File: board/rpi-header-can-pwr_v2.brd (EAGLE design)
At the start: 87 x 56.5 mm, 43 parts, among them U1 MCP2515, X1 RJ45-8L21-S, X2 RASPI_BOARD_B+#_E3

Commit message: add board temp sensor add battery voltage sensor
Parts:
- added C13, C15: 100n, rcl:C0603
- added C14: 1u, rcl:C0603
- added R7: 0, resistor:R0603
- added R8, R9: 4.7K, resistor:R0603
- added U2: ADS1015, SparkFun-IC-Conversion:MSOP10
- added U3: BME280, SparkFun-Sensors:LGA-8-2.5X2.5
- moved R4 25.5 mm to (24.5, 52.5), turned to 90 degrees
- moved D2 21.6 mm to (21.0, 49.0), turned to 90 degrees
- moved D3 15.8 mm to (24.5, 47.5), turned to 180 degrees
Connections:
- new net ADC_ALERT: R7.1, X2.40
- new net ADC_INPUT_1: U2.4
- new net I2C_SCL: R9.2, U2.10, U3.4, X2.5
- new net I2C_SDA: R8.2, U2.9, U3.3, X2.3
- new net N$9: R7.2, U2.2
- net +3V3: now also C13.1, C14.1, C15.1, R8.1, R9.1, U2.8, U3.2, U3.6, U3.8
- net GND: now also C13.2, C14.2, C15.2, U2.1, U2.3, U3.1, U3.5, U3.7
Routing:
- net I2C_SCL: track 0.00 -> 71.5 mm, vias 0 -> 2
- net I2C_SDA: track 0.00 -> 62.5 mm
- net +3V3: track 178.3 -> 227.6 mm, vias 2 -> 3
- net N$9: track 0.00 -> 24.1 mm
- net ADC_ALERT: track 0.00 -> 11.6 mm
- net 5V: track 33.3 -> 22.7 mm
- net GND: track 13.7 -> 21.1 mm, vias 203 -> 211
- net TAMPER: track 34.2 -> 39.6 mm
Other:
- board text added: "ADC ALERT"
- board text added: "ADS1x15"
- board text added: "BME280"
- board text added: "T2"
- board text added: "i2c pullups"

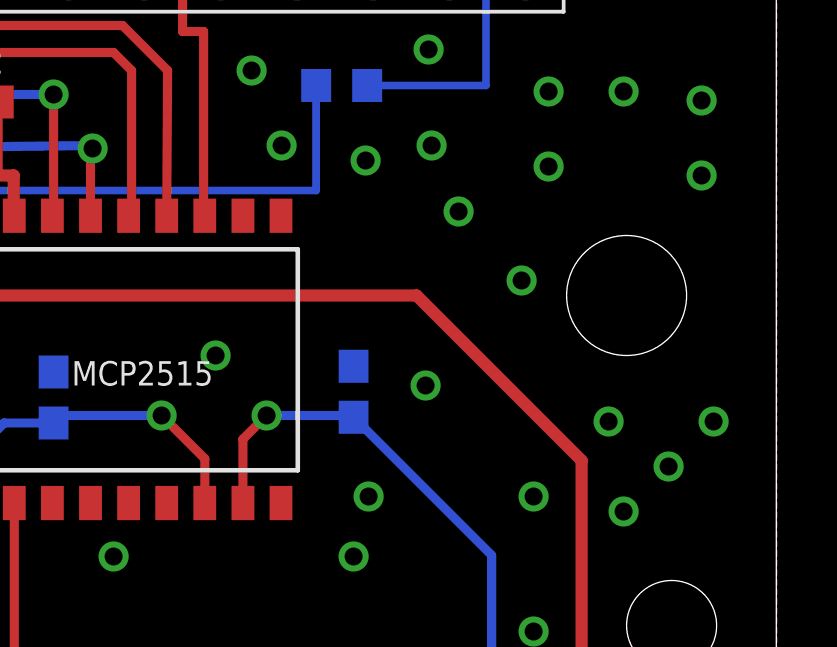
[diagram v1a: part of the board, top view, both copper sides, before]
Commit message: ADC ALERT requires pull up
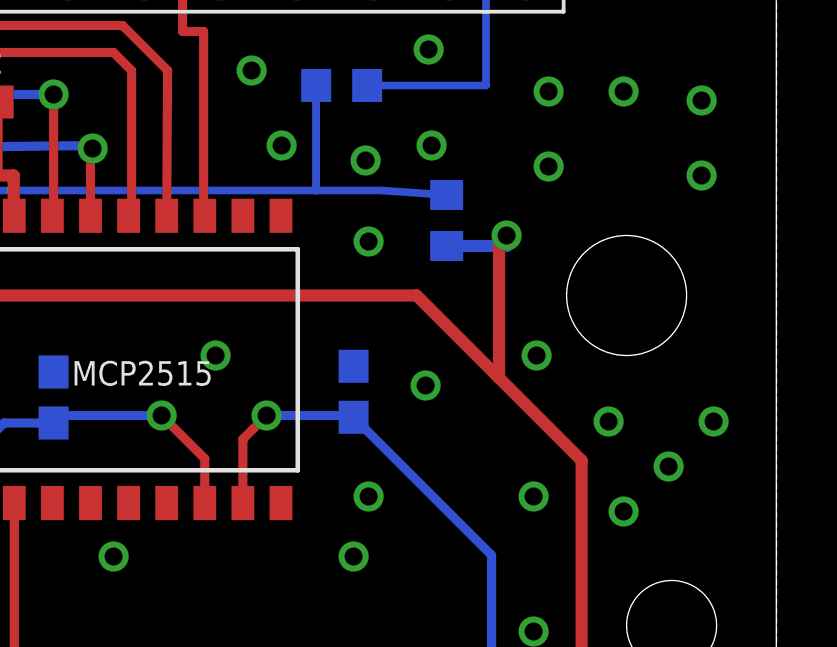
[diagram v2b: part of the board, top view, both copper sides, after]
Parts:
- added R10: 4.7K, resistor:R0603
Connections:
- net +3V3: now also R10.2
- net N$9: now also R10.1
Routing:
- net +3V3: track 227.6 -> 234.9 mm, vias 3 -> 4
- net N$9: track 24.1 -> 28.5 mm
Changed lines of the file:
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@@
 <text x="5.3" y="52.7" size="1.4224" layer="122" rot="MR270">12V</text>
 <text x="18.5" y="48.8" size="1.4224" layer="122" rot="MR90">GND</text>
+<text x="76.4" y="40.3" size="0.8128" layer="122" rot="MR0">R1</text>
 </plain>
 <attributes>
@@
 <element name="C14" library="rcl" package="C0603" value="1u" x="31.5" y="21" rot="MR0"/>
 <element name="C15" library="rcl" package="C0603" value="100n" x="31.54" y="18.82" rot="MR0"/>
+<element name="R10" library="resistor" package="R0603" value="4.7K" x="76" y="43" rot="MR270"/>
 </elements>
 <signals>
@@
 <wire x1="77.5" y1="24.5" x2="80.5" y2="24.5" width="0.4064" layer="1"/>
 <wire x1="80.5" y1="24.5" x2="80.5" y2="35" width="0.4064" layer="1"/>
-<wire x1="80.5" y1="35" x2="75" y2="40.5" width="0.4064" layer="1"/>
+<wire x1="80.5" y1="35" x2="77.75" y2="37.75" width="0.4064" layer="1"/>
+<wire x1="77.75" y1="37.75" x2="75" y2="40.5" width="0.4064" layer="1"/>
 <wire x1="75" y1="40.5" x2="60.32" y2="40.5" width="0.4064" layer="1"/>
 <wire x1="60.32" y1="40.5" x2="60.32" y2="43.1579" width="0.4064" layer="1"/>
@@
 <via x="26" y="25" extent="1-16" drill="0.6"/>
 <wire x1="26" y1="25" x2="26" y2="26.5" width="0.254" layer="1"/>
+<contactref element="R10" pad="2"/>
+<wire x1="76" y1="42.15" x2="78" y2="42.15" width="0.4064" layer="16"/>
+<wire x1="78" y1="42.15" x2="78" y2="42.5" width="0.4064" layer="16"/>
+<via x="78" y="42.5" extent="1-16" drill="0.6"/>
+<wire x1="78" y1="42.5" x2="77.75" y2="42.5" width="0.4064" layer="1"/>
+<wire x1="77.75" y1="42.5" x2="77.75" y2="37.75" width="0.4064" layer="1"/>
 </signal>
 <signal name="GND">
@@
 <via x="81.9" y="47.3" extent="1-16" drill="0.6"/>
 <via x="79.4" y="44.8" extent="1-16" drill="0.6"/>
-<via x="76.4" y="43.3" extent="1-16" drill="0.6"/>
+<via x="73.4" y="42.3" extent="1-16" drill="0.6"/>
 <via x="83.4" y="34.8" extent="1-16" drill="0.6"/>
 <via x="84.9" y="36.3" extent="1-16" drill="0.6"/>
@@
 <via x="85" y="18.6" extent="1-16" drill="0.6"/>
 <via x="84.5" y="44.5" extent="1-16" drill="0.6"/>
-<via x="78.5" y="41" extent="1-16" drill="0.6"/>
+<via x="79" y="38.5" extent="1-16" drill="0.6"/>
 <via x="47.9" y="48.9" extent="1-16" drill="0.6"/>
 <via x="35.9" y="38.4" extent="1-16" drill="0.6"/>
@@
 <wire x1="54.5" y1="44" x2="71.65" y2="44" width="0.254" layer="16"/>
 <wire x1="71.65" y1="44" x2="71.65" y2="47.5" width="0.254" layer="16"/>
+<contactref element="R10" pad="1"/>
+<wire x1="76" y1="43.85" x2="73.85" y2="44" width="0.254" layer="16"/>
+<wire x1="73.85" y1="44" x2="71.65" y2="44" width="0.254" layer="16"/>
 </signal>
 </signals>

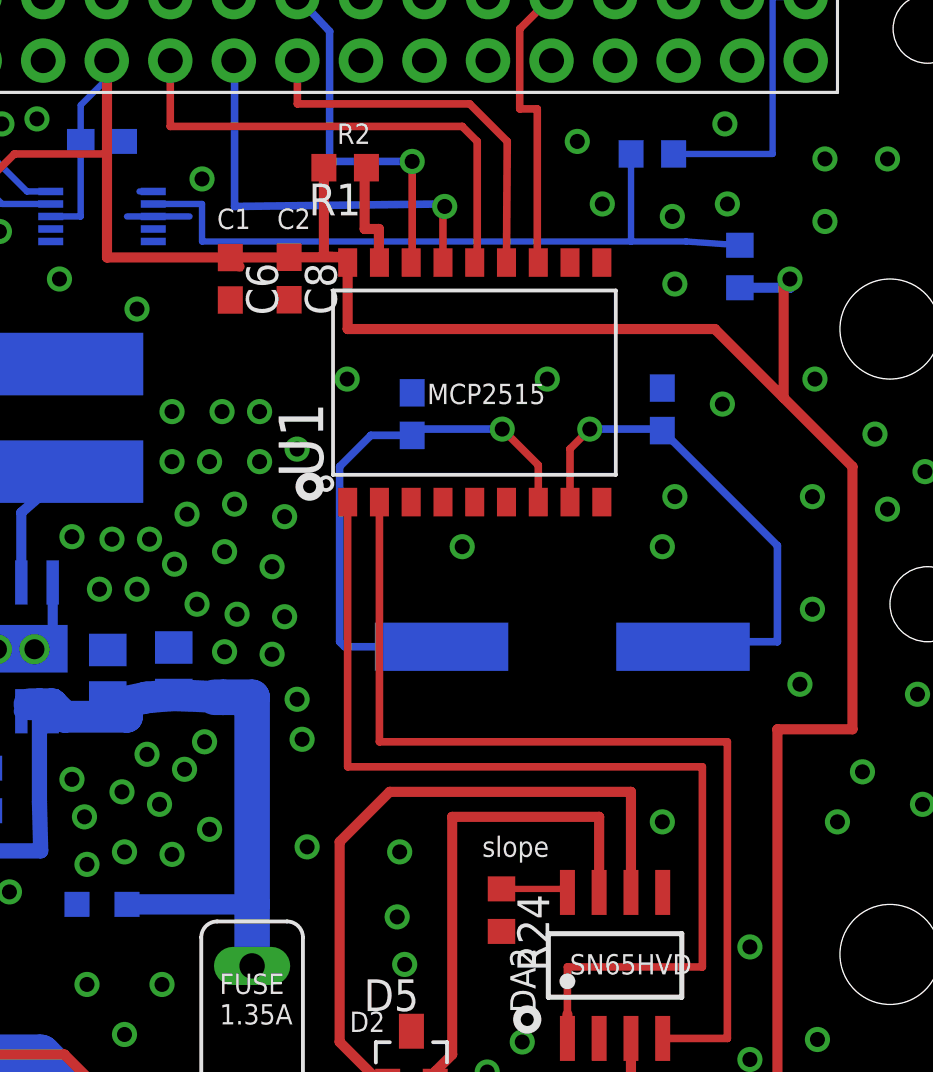
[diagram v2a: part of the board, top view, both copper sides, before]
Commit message: add voltage divider and gpio protection to battery voltage sensor
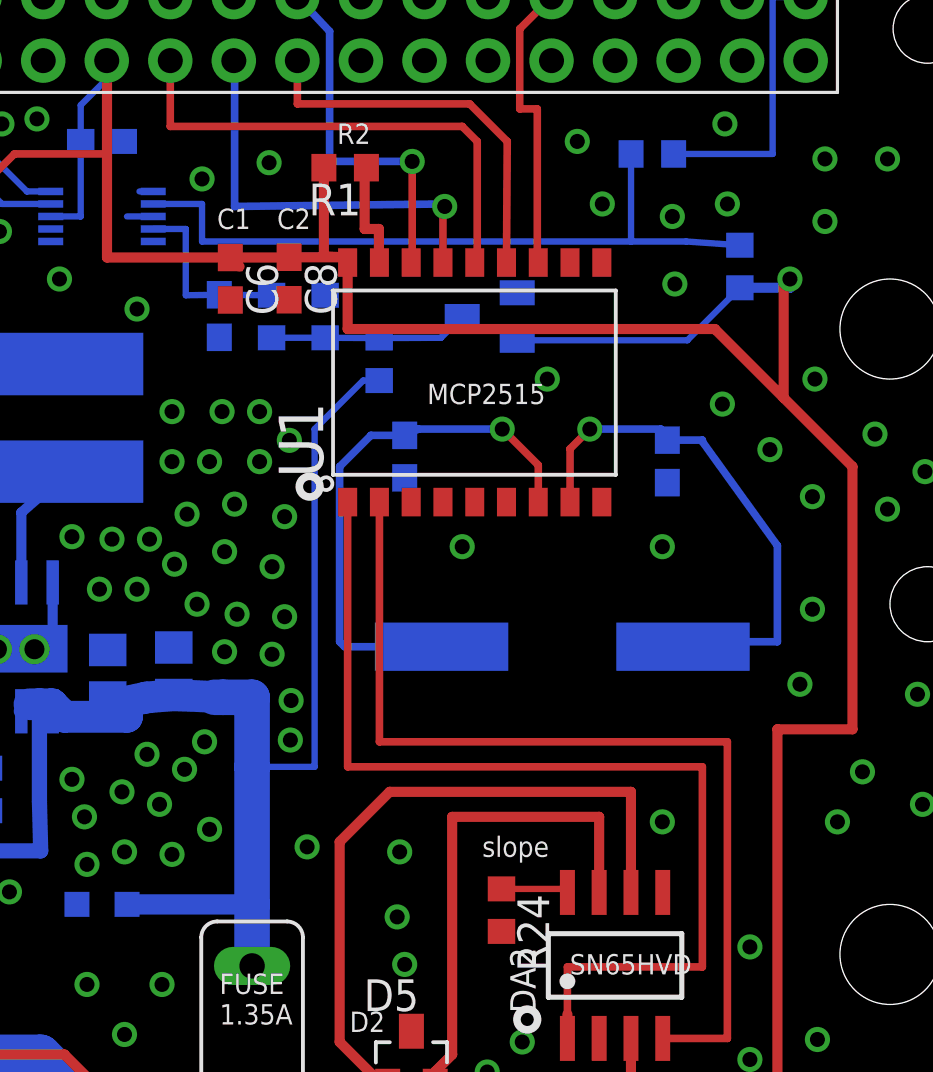
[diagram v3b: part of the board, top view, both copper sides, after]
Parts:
- added C29: 10nF, eagle-ltspice:C0603
- added D7: BAS70-04, diode:SOT23
- added R20: 68k, rcl:R0603
- added R21: 20k, rcl:R0603
- added R22: 1k, rcl:R0603
- moved C2 2.09 mm to (73.1, 35.2), turned to 90 degrees
- moved C1 1.73 mm to (62.6, 35.4), turned to 90 degrees
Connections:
- new net 12V_REFERENCE4: D7.3, R20.2, R21.2, R22.1
- net +12V: now also R20.1
- net +3V3: now also D7.2
- net ADC_INPUT_1: now also C29.2, R22.2
- net GND: now also C29.1, D7.1, R21.1
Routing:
- net +12V: track 75.9 -> 95.3 mm
- net +3V3: track 234.9 -> 244.7 mm
- net 12V_REFERENCE4: track 0.00 -> 7.97 mm
- net ADC_INPUT_1: track 0.00 -> 7.38 mm
- net GND: track 21.1 -> 19.6 mm
- net N$2: track 20.4 -> 20.9 mm
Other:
- board text added: "R13"
- board text added: "R14"
- board text added: "crystal cap"
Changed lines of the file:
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@@
 <text x="18.5" y="48.8" size="1.4224" layer="122" rot="MR90">GND</text>
 <text x="76.4" y="40.3" size="0.8128" layer="122" rot="MR0">R1</text>
+<text x="55.97" y="38.36" size="0.8128" layer="122" rot="MR0">C9</text>
+<text x="58.14" y="38.3" size="0.8128" layer="122" rot="MR0">R5</text>
+<text x="67.25" y="38.21" size="0.8128" layer="122" rot="MR0">D4</text>
+<text x="62.52" y="41.29" size="0.8128" layer="122" rot="MR0">R13</text>
+<text x="60.46" y="42.73" size="0.8128" layer="122" rot="MR0">R14</text>
+<text x="70.75" y="34.21" size="0.8128" layer="122" rot="MR0">crystal cap</text>
 </plain>
 <attributes>
@@
 <attribute name="PROD_ID" value="IC-09906" x="65.4" y="39.64" size="1.778" layer="27" display="off"/>
 </element>
-<element name="C1" library="SparkFun-Capacitors" package="0603-CAP" value="22pF" x="62.9" y="37.1" rot="MR270">
-<attribute name="PROD_ID" value="CAP-07876" x="61.63" y="44.72" size="1.778" layer="28" rot="MR270" display="off"/>
-</element>
-<element name="C2" library="SparkFun-Capacitors" package="0603-CAP" value="22pF" x="72.9" y="37.29" rot="MR270">
-<attribute name="PROD_ID" value="CAP-07876" x="75.44" y="48.72" size="1.778" layer="28" rot="MR270" display="off"/>
+<element name="C1" library="SparkFun-Capacitors" package="0603-CAP" value="22pF" x="62.6" y="35.4" rot="MR90">
+<attribute name="PROD_ID" value="CAP-07876" x="63.87" y="27.78" size="1.778" layer="28" rot="MR90" display="off"/>
+</element>
+<element name="C2" library="SparkFun-Capacitors" package="0603-CAP" value="22pF" x="73.1" y="35.21" rot="MR90">
+<attribute name="PROD_ID" value="CAP-07876" x="70.56" y="23.78" size="1.778" layer="28" rot="MR90" display="off"/>
 </element>
 <element name="C3" library="rcl" package="C0603" value="100n" x="72.48" y="8.87" rot="R270"/>
@@
 <element name="C15" library="rcl" package="C0603" value="100n" x="31.54" y="18.82" rot="MR0"/>
 <element name="R10" library="resistor" package="R0603" value="4.7K" x="76" y="43" rot="MR270"/>
+<element name="R20" library="rcl" package="R0603" value="68k" x="61.58" y="39.29" rot="MR90"/>
+<element name="R21" library="rcl" package="R0603" value="20k" x="59.42" y="41" rot="MR270"/>
+<element name="D7" library="diode" package="SOT23" value="BAS70-04" x="66" y="41" rot="MR270"/>
+<element name="C29" library="eagle-ltspice" package="C0603" value="10nF" x="55.19" y="41.02" rot="MR90">
+<attribute name="SPICEPREFIX" value="C" x="45.19" y="41.02" size="1.778" layer="28" rot="MR90" display="off"/>
+<attribute name="SPICEMODEL" value="NONE" x="45.19" y="41.02" size="1.778" layer="28" rot="MR90" display="off"/>
+</element>
+<element name="R22" library="rcl" package="R0603" value="1k" x="57.28" y="41" rot="MR90"/>
 </elements>
 <signals>
@@
 <wire x1="78" y1="42.5" x2="77.75" y2="42.5" width="0.4064" layer="1"/>
 <wire x1="77.75" y1="42.5" x2="77.75" y2="37.75" width="0.4064" layer="1"/>
+<contactref element="D7" pad="2"/>
+<wire x1="67.1" y1="40.05" x2="73.9" y2="40.05" width="0.254" layer="16"/>
+<wire x1="73.9" y1="40.05" x2="76" y2="42.15" width="0.254" layer="16"/>
 </signal>
 <signal name="GND">
@@
 <contactref element="D3" pad="2"/>
 <via x="62.4" y="19.6" extent="1-16" drill="0.6"/>
-<via x="58.3" y="35.7" extent="1-16" drill="0.6"/>
+<via x="57.99" y="36.05" extent="1-16" drill="0.6"/>
 <via x="41.8" y="26" extent="1-16" drill="0.6"/>
 <via x="42.8" y="27.5" extent="1-16" drill="0.6"/>
@@
 <via x="53.3" y="19.5" extent="1-16" drill="0.6"/>
 <via x="44.3" y="18" extent="1-16" drill="0.6"/>
-<via x="58.5" y="24.1" extent="1-16" drill="0.6"/>
+<via x="58.03" y="24.07" extent="1-16" drill="0.6"/>
 <via x="57.8" y="29" extent="1-16" drill="0.6"/>
 <via x="79.1" y="12.1" extent="1-16" drill="0.6"/>
@@
 <via x="72.3" y="2" extent="1-16" drill="0.6"/>
 <via x="62.3" y="3" extent="1-16" drill="0.6"/>
-<via x="60.3" y="38.5" extent="1-16" drill="0.6"/>
+<via x="77.2" y="35.68" extent="1-16" drill="0.6"/>
 <via x="68.3" y="38.5" extent="1-16" drill="0.6"/>
 <via x="75.3" y="37.5" extent="1-16" drill="0.6"/>
@@
 <contactref element="D18" pad="1"/>
 <contactref element="X1" pad="8"/>
-<via x="58.3" y="25.7" extent="1-16" drill="0.6"/>
+<via x="58.06" y="25.65" extent="1-16" drill="0.6"/>
 <via x="54.6" y="24" extent="1-16" drill="0.6"/>
 <via x="62.6" y="15.1" extent="1-16" drill="0.6"/>
@@
 <via x="81.9" y="33.3" extent="1-16" drill="0.6"/>
 <via x="72.9" y="31.8" extent="1-16" drill="0.6"/>
-<via x="73.4" y="33.8" extent="1-16" drill="0.6"/>
+<via x="57.18" y="47.15" extent="1-16" drill="0.6"/>
 <via x="64.9" y="31.8" extent="1-16" drill="0.6"/>
 <via x="78.9" y="33.8" extent="1-16" drill="0.6"/>
@@
 <contactref element="U2" pad="3"/>
 <contactref element="U2" pad="1"/>
-<wire x1="52.55" y1="45" x2="54" y2="45" width="0.254" layer="16"/>
 <wire x1="52.55" y1="45" x2="51.5" y2="45" width="0.254" layer="16"/>
 <wire x1="52.55" y1="46" x2="52" y2="46" width="0.254" layer="16"/>
@@
 <wire x1="35.9" y1="38.4" x2="36.67" y2="38.4" width="0.3048" layer="1"/>
 <wire x1="36.67" y1="38.4" x2="39.2" y2="40.93" width="0.3048" layer="1"/>
+<contactref element="C29" pad="1"/>
+<contactref element="D7" pad="1"/>
+<contactref element="R21" pad="1"/>
 </signal>
 <signal name="CAN_TX">
@@
 <wire x1="69.21" y1="35.71" x2="70" y2="36.5" width="0.3048" layer="1"/>
 <via x="70" y="36.5" extent="1-16" drill="0.6"/>
-<wire x1="72.9" y1="36.44" x2="72.84" y2="36.5" width="0.3048" layer="16"/>
+<wire x1="73.1" y1="36.06" x2="72.84" y2="36.5" width="0.3048" layer="16"/>
 <wire x1="72.84" y1="36.5" x2="70" y2="36.5" width="0.3048" layer="16"/>
-<wire x1="72.9" y1="36.44" x2="77.5" y2="31.84" width="0.3048" layer="16"/>
+<wire x1="73.1" y1="36.06" x2="74.5" y2="36.06" width="0.3048" layer="16"/>
+<wire x1="74.5" y1="36.06" x2="74.5" y2="36" width="0.3048" layer="16"/>
+<wire x1="74.5" y1="36" x2="77.5" y2="31.84" width="0.3048" layer="16"/>
 <wire x1="77.5" y1="31.84" x2="77.5" y2="28" width="0.3048" layer="16"/>
 <wire x1="77.5" y1="28" x2="73.926" y2="28" width="0.3048" layer="16"/>
@@
 <wire x1="60.2" y1="27.8" x2="60" y2="28" width="0.3048" layer="16"/>
 <wire x1="60" y1="28" x2="60" y2="35" width="0.3048" layer="16"/>
-<wire x1="62.9" y1="36.25" x2="61.25" y2="36.25" width="0.3048" layer="16"/>
+<wire x1="62.6" y1="36.25" x2="61.25" y2="36.25" width="0.3048" layer="16"/>
 <wire x1="61.25" y1="36.25" x2="60" y2="35" width="0.3048" layer="16"/>
 <wire x1="67.94" y1="33.5821" x2="67.94" y2="35.06" width="0.3048" layer="1"/>
@@
 <via x="66.5" y="36.5" extent="1-16" drill="0.6"/>
 <wire x1="66.5" y1="36.5" x2="63.15" y2="36.5" width="0.3048" layer="16"/>
-<wire x1="63.15" y1="36.5" x2="62.9" y2="36.25" width="0.3048" layer="16"/>
+<wire x1="63.15" y1="36.5" x2="62.6" y2="36.25" width="0.3048" layer="16"/>
 </signal>
 <signal name="+12V">
@@
 <contactref element="R6" pad="1"/>
 <wire x1="55.34531875" y1="25.778828125" x2="56.5" y2="25.778828125" width="1.4224" layer="16"/>
-<wire x1="56.5" y1="25.778828125" x2="56.5" y2="17.5" width="1.4224" layer="16"/>
+<wire x1="56.5" y1="25.778828125" x2="56.5" y2="23" width="1.4224" layer="16"/>
+<wire x1="56.5" y1="23" x2="56.5" y2="17.5" width="1.4224" layer="16"/>
 <wire x1="56.5" y1="17.5" x2="56.5" y2="15.04" width="1.4224" layer="16"/>
 <wire x1="51.5" y1="17.5" x2="56.5" y2="17.5" width="0.8128" layer="16"/>
+<contactref element="R20" pad="1"/>
+<wire x1="56.5" y1="23" x2="59" y2="23" width="0.254" layer="16"/>
+<wire x1="59" y1="23" x2="59" y2="36.5" width="0.254" layer="16"/>
+<wire x1="59" y1="36.5" x2="60.94" y2="38.44" width="0.254" layer="16"/>
+<wire x1="60.94" y1="38.44" x2="61.58" y2="38.44" width="0.254" layer="16"/>
 </signal>
 <signal name="N$1">
@@
 <signal name="ADC_INPUT_1">
 <contactref element="U2" pad="4"/>
+<contactref element="C29" pad="2"/>
+<contactref element="R22" pad="2"/>
+<wire x1="52.55" y1="44.5" x2="53.85" y2="44.5" width="0.254" layer="16"/>
+<wire x1="53.85" y1="44.5" x2="53.85" y2="41.85" width="0.254" layer="16"/>
+<wire x1="53.85" y1="41.85" x2="55.19" y2="41.87" width="0.254" layer="16"/>
+<wire x1="55.19" y1="41.87" x2="57.28" y2="41.85" width="0.254" layer="16"/>
 </signal>
 <signal name="ADC_ALERT">
@@
 <wire x1="73.85" y1="44" x2="71.65" y2="44" width="0.254" layer="16"/>
 </signal>
+<signal name="12V_REFERENCE4">
+<contactref element="R20" pad="2"/>
+<contactref element="R21" pad="2"/>
+<contactref element="D7" pad="3"/>
+<contactref element="R22" pad="1"/>
+<wire x1="57.28" y1="40.15" x2="59.42" y2="40.15" width="0.254" layer="16"/>
+<wire x1="59.42" y1="40.15" x2="61.58" y2="40.14" width="0.254" layer="16"/>
+<wire x1="61.58" y1="40.14" x2="64.05" y2="40.15" width="0.254" layer="16"/>
+<wire x1="64.05" y1="40.15" x2="64.9" y2="41" width="0.254" layer="16"/>
+</signal>
 </signals>
